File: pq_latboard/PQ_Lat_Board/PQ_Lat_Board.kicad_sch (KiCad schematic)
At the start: 20 parts, among them IC1 TCN75AVOA713, J1 Conn_01x11_MountingPin, J2 connector-coax

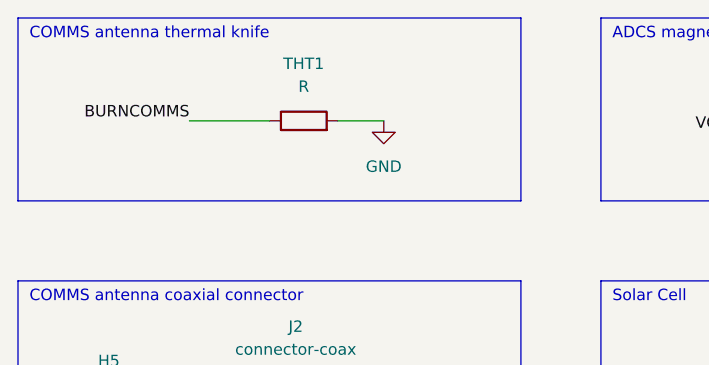
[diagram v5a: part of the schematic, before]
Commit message: BOM creation schematic changes 2.0
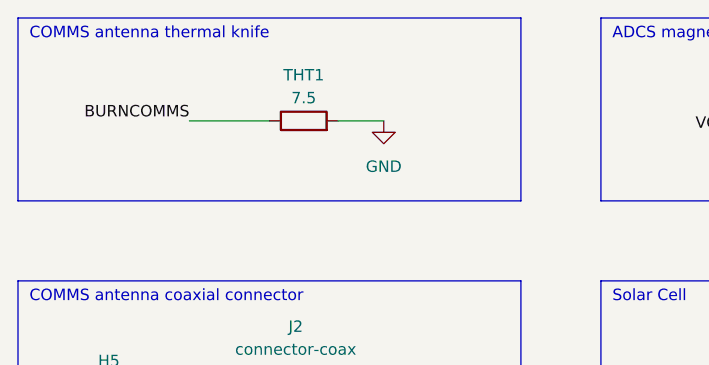
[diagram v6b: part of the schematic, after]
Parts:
- D1: Manufacturer 1 (none) -> Advanced Photonix; Manufacturer Part Number 1 (none) -> SLCD-61N8; Supplier 1 (none) -> Farnell; Supplier Part Number 1 (none) -> 1218991
- H1, H2, H3, H4, H5, NT1: Manufacturer 1 (none) -> N/A; Manufacturer Part Number 1 (none) -> N/A; Supplier 1 (none) -> N/A; Supplier Part Number 1 (none) -> N/A
- IC1: Manufacturer 1 (none) -> Microchip; Manufacturer Part Number 1 (none) -> TCN75AVOA; Supplier 1 (none) -> Mouser; Supplier Part Number 1 (none) -> 579-TCN75AVOA
- J1: Manufacturer 1 (none) -> Molex; Manufacturer Part Number 1 (none) -> PicoBlade_53261; Supplier 1 (none) -> Mouser; Supplier Part Number 1 (none) -> 538-53261-7006
- J2: Manufacturer 1 (none) -> Hirose; Manufacturer Part Number 1 (none) -> C.FL-R-SMT-1; Supplier 1 (none) -> Mouser; Supplier Part Number 1 (none) -> 798-CFL-R-SMT-190
- SC1: Manufacturer 1 (none) -> Azur Space; Manufacturer Part Number 1 (none) -> 3G30A; Supplier 1 (none) -> Lighttricity; Supplier Part Number 1 (none) -> N/A
- THT1: value R -> 7.5; Manufacturer 1 (none) -> Vishay/Dale; Manufacturer Part Number 1 (none) -> MRS25000C7508FCT00; Supplier 1 (none) -> Mouser; Supplier Part Number 1 (none) -> 594-MRS25000C7508FCT
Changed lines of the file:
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@@
   (symbol (lib_id "Device:R") (at 81.28 64.77 90) (unit 1)
     (in_bom yes) (on_board yes) (dnp no) (fields_autoplaced)
-    (property "Reference" "THT1" (at 81.28 58.42 90)
-      (effects (font (size 1.27 1.27)))
-    )
-    (property "Value" "R" (at 81.28 60.96 90)
+    (property "Reference" "THT1" (at 81.28 59.69 90)
+      (effects (font (size 1.27 1.27)))
+    )
+    (property "Value" "7.5" (at 81.28 62.23 90)
       (effects (font (size 1.27 1.27)))
     )
@@
     )
     (property "Datasheet" "~" (at 81.28 64.77 0)
+      (effects (font (size 1.27 1.27)) hide)
+    )
+    (property "Manufacturer 1" "Vishay/Dale" (at 81.28 64.77 0)
+      (effects (font (size 1.27 1.27)) hide)
+    )
+    (property "Manufacturer Part Number 1" "MRS25000C7508FCT00 " (at 81.28 64.77 0)
+      (effects (font (size 1.27 1.27)) hide)
+    )
+    (property "Supplier 1" "Mouser" (at 81.28 64.77 0)
+      (effects (font (size 1.27 1.27)) hide)
+    )
+    (property "Supplier Part Number 1" "594-MRS25000C7508FCT " (at 81.28 64.77 0)
       (effects (font (size 1.27 1.27)) hide)
     )
@@
       (effects (font (size 1.27 1.27)) hide)
     )
+    (property "Manufacturer 1" "N/A" (at 55.88 95.25 0)
+      (effects (font (size 1.27 1.27)) hide)
+    )
+    (property "Manufacturer Part Number 1" "N/A" (at 55.88 95.25 0)
+      (effects (font (size 1.27 1.27)) hide)
+    )
+    (property "Supplier 1" "N/A" (at 55.88 95.25 0)
+      (effects (font (size 1.27 1.27)) hide)
+    )
+    (property "Supplier Part Number 1" "N/A" (at 55.88 95.25 0)
+      (effects (font (size 1.27 1.27)) hide)
+    )
     (pin "1")
     (instances
@@
       (effects (font (size 1.27 1.27)) hide)
     )
+    (property "Manufacturer 1" "N/A" (at 82.55 120.65 0)
+      (effects (font (size 1.27 1.27)) hide)
+    )
+    (property "Manufacturer Part Number 1" "N/A" (at 82.55 120.65 0)
+      (effects (font (size 1.27 1.27)) hide)
+    )
+    (property "Supplier 1" "N/A" (at 82.55 120.65 0)
+      (effects (font (size 1.27 1.27)) hide)
+    )
+    (property "Supplier Part Number 1" "N/A" (at 82.55 120.65 0)
+      (effects (font (size 1.27 1.27)) hide)
+    )
     (pin "1")
     (instances
@@
     )
     (property "Datasheet" "" (at 140.97 103.124 0)
+      (effects (font (size 1.27 1.27)) hide)
+    )
+    (property "Manufacturer 1" "Azur Space" (at 142.494 92.71 0)
+      (effects (font (size 1.27 1.27)) hide)
+    )
+    (property "Manufacturer Part Number 1" "3G30A" (at 142.494 92.71 0)
+      (effects (font (size 1.27 1.27)) hide)
+    )
+    (property "Supplier 1" "Lighttricity" (at 142.494 92.71 0)
+      (effects (font (size 1.27 1.27)) hide)
+    )
+    (property "Supplier Part Number 1" "N/A" (at 142.494 92.71 0)
       (effects (font (size 1.27 1.27)) hide)
     )
@@
       (effects (font (size 1.27 1.27)) hide)
     )
+    (property "Manufacturer 1" "N/A" (at 58.42 134.62 0)
+      (effects (font (size 1.27 1.27)) hide)
+    )
+    (property "Manufacturer Part Number 1" "N/A" (at 58.42 134.62 0)
+      (effects (font (size 1.27 1.27)) hide)
+    )
+    (property "Supplier 1" "N/A" (at 58.42 134.62 0)
+      (effects (font (size 1.27 1.27)) hide)
+    )
+    (property "Supplier Part Number 1" "N/A" (at 58.42 134.62 0)
+      (effects (font (size 1.27 1.27)) hide)
+    )
     (pin "1")
     (instances
@@
     (property "BOM_MANUFACTURER PART" "" (at 190.5 109.22 0)
       (effects (font (size 1.27 1.27)) (justify left bottom) hide)
+    )
+    (property "Manufacturer 1" "Microchip" (at 190.5 109.22 0)
+      (effects (font (size 1.27 1.27)) hide)
+    )
+    (property "Manufacturer Part Number 1" "TCN75AVOA" (at 190.5 109.22 0)
+      (effects (font (size 1.27 1.27)) hide)
+    )
+    (property "Supplier 1" "Mouser" (at 190.5 109.22 0)
+      (effects (font (size 1.27 1.27)) hide)
+    )
+    (property "Supplier Part Number 1" " 579-TCN75AVOA" (at 190.5 109.22 0)
+      (effects (font (size 1.27 1.27)) hide)
     )
     (pin "1")
@@
       (effects (font (size 1.27 1.27)) hide)
     )
+    (property "Manufacturer 1" "N/A" (at 82.55 134.62 0)
+      (effects (font (size 1.27 1.27)) hide)
+    )
+    (property "Manufacturer Part Number 1" "N/A" (at 82.55 134.62 0)
+      (effects (font (size 1.27 1.27)) hide)
+    )
+    (property "Supplier 1" "N/A" (at 82.55 134.62 0)
+      (effects (font (size 1.27 1.27)) hide)
+    )
+    (property "Supplier Part Number 1" "N/A" (at 82.55 134.62 0)
+      (effects (font (size 1.27 1.27)) hide)
+    )
     (pin "1")
     (instances
@@
       (effects (font (size 1.27 1.27)) hide)
     )
+    (property "Manufacturer 1" "N/A" (at 143.51 66.04 0)
+      (effects (font (size 1.27 1.27)) hide)
+    )
+    (property "Manufacturer Part Number 1" "N/A" (at 143.51 66.04 0)
+      (effects (font (size 1.27 1.27)) hide)
+    )
+    (property "Supplier 1" "N/A" (at 143.51 66.04 0)
+      (effects (font (size 1.27 1.27)) hide)
+    )
+    (property "Supplier Part Number 1" "N/A" (at 143.51 66.04 0)
+      (effects (font (size 1.27 1.27)) hide)
+    )
     (pin "1")
     (pin "2")
@@
       (effects (font (size 1.27 1.27)) hide)
     )
+    (property "Manufacturer 1" "N/A" (at 58.42 120.65 0)
+      (effects (font (size 1.27 1.27)) hide)
+    )
+    (property "Manufacturer Part Number 1" "N/A" (at 58.42 120.65 0)
+      (effects (font (size 1.27 1.27)) hide)
+    )
+    (property "Supplier 1" "N/A" (at 58.42 120.65 0)
+      (effects (font (size 1.27 1.27)) hide)
+    )
+    (property "Supplier Part Number 1" "N/A" (at 58.42 120.65 0)
+      (effects (font (size 1.27 1.27)) hide)
+    )
     (pin "1")
     (instances
@@
       (effects (font (size 1.27 1.27)) hide)
     )
+    (property "Manufacturer 1" "Advanced Photonix" (at 214.376 64.77 0)
+      (effects (font (size 1.27 1.27)) hide)
+    )
+    (property "Manufacturer Part Number 1" "SLCD-61N8" (at 214.376 64.77 0)
+      (effects (font (size 1.27 1.27)) hide)
+    )
+    (property "Supplier 1" "Farnell" (at 214.376 64.77 0)
+      (effects (font (size 1.27 1.27)) hide)
+    )
+    (property "Supplier Part Number 1" "1218991" (at 214.376 64.77 0)
+      (effects (font (size 1.27 1.27)) hide)
+    )
     (pin "1")
     (pin "2")
@@
     )
     (property "Datasheet" "~" (at 139.7 129.54 0)
+      (effects (font (size 1.27 1.27)) hide)
+    )
+    (property "Manufacturer 1" "Molex" (at 139.7 129.54 0)
+      (effects (font (size 1.27 1.27)) hide)
+    )
+    (property "Manufacturer Part Number 1" "PicoBlade_53261" (at 139.7 129.54 0)
+      (effects (font (size 1.27 1.27)) hide)
+    )
+    (property "Supplier 1" "Mouser" (at 139.7 129.54 0)
+      (effects (font (size 1.27 1.27)) hide)
+    )
+    (property "Supplier Part Number 1" "538-53261-7006" (at 139.7 129.54 0)
       (effects (font (size 1.27 1.27)) hide)
     )
@@
       (effects (font (size 1.27 1.27)) hide)
     )
+    (property "Manufacturer 1" "Hirose" (at 80.01 93.98 0)
+      (effects (font (size 1.27 1.27)) hide)
+    )
+    (property "Manufacturer Part Number 1" "C.FL-R-SMT-1" (at 80.01 93.98 0)
+      (effects (font (size 1.27 1.27)) hide)
+    )
+    (property "Supplier 1" "Mouser" (at 80.01 93.98 0)
+      (effects (font (size 1.27 1.27)) hide)
+    )
+    (property "Supplier Part Number 1" "798-CFL-R-SMT-190 " (at 80.01 93.98 0)
+      (effects (font (size 1.27 1.27)) hide)
+    )

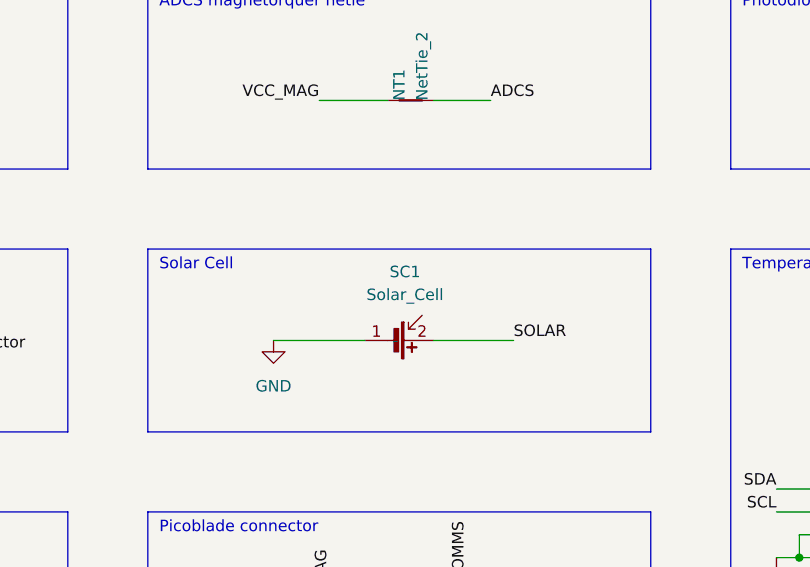
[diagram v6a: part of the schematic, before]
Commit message: Updated outer boards design as required by the change from Azur Space house-cut solar cells to Lighttricity's S3040_CIC model. Preserved the older design in lat_board_old
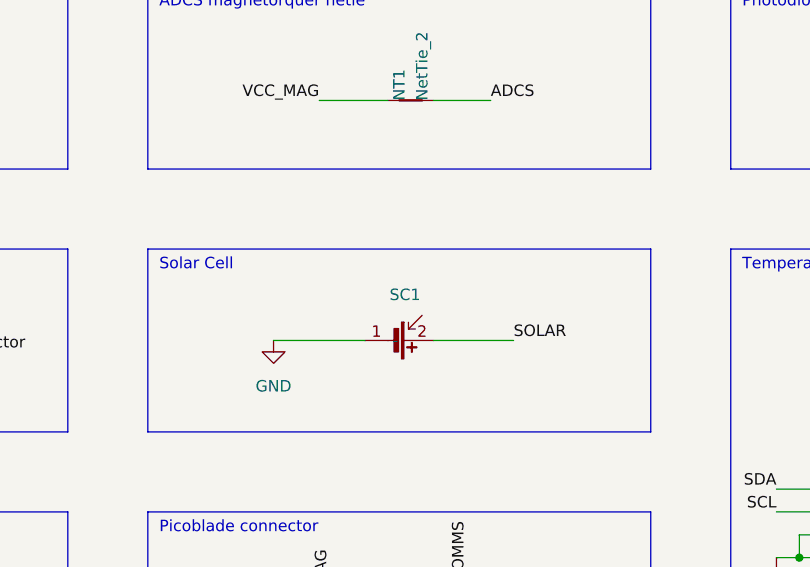
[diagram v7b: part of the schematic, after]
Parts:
- removed SC1: Solar_Cell, -nsl_power:Azur-Space-PQ-cut-SC, symbol power-nsl:Solar_Cell
- added SC1: ~, power-nsl:Lighttricity_S3040_CIC, symbol power-nsl:S3040_CIC
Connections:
- net GND: now also SC1.1 (-)
- net SOLAR: now also SC1.2
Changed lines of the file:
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@@
-    )
-  )
-  (symbol (lib_id "power-nsl:Solar_Cell") (at 142.494 92.71 270) (unit 1)
-    (in_bom yes) (on_board yes) (dnp no) (fields_autoplaced)
-    (property "Reference" "SC1" (at 142.875 85.09 90)
-      (effects (font (size 1.27 1.27)))
-    )
-    (property "Value" "Solar_Cell" (at 142.875 87.63 90)
-      (effects (font (size 1.27 1.27)))
-    )
-    (property "Footprint" "-nsl_power:Azur-Space-PQ-cut-SC" (at 140.97 103.124 0)
-      (effects (font (size 1.27 1.27)) hide)
-    )
-    (property "Datasheet" "" (at 140.97 103.124 0)
-      (effects (font (size 1.27 1.27)) hide)
-    )
-    (property "Manufacturer 1" "Azur Space" (at 142.494 92.71 0)
-      (effects (font (size 1.27 1.27)) hide)
-    )
-    (property "Manufacturer Part Number 1" "3G30A" (at 142.494 92.71 0)
-      (effects (font (size 1.27 1.27)) hide)
-    )
-    (property "Supplier 1" "Lighttricity" (at 142.494 92.71 0)
-      (effects (font (size 1.27 1.27)) hide)
-    )
-    (property "Supplier Part Number 1" "N/A" (at 142.494 92.71 0)
-      (effects (font (size 1.27 1.27)) hide)
-    )
-    (pin "1")
-    (pin "2")
-    (instances
-      (project "PQ_Lat_Board"
-        (path "/4da848d5-e65a-4ace-88f8-d9d6d6b9afa2"
-          (reference "SC1") (unit 1)
-        )
-      )
     )
   )
@@
         )
       )
+    )
+  )
+  (symbol (lib_id "power-nsl:S3040_CIC") (at 142.24 92.71 270) (unit 1)
+    (in_bom yes) (on_board yes) (dnp no) (fields_autoplaced)
+    (property "Reference" "SC1" (at 142.875 87.63 90)
+      (effects (font (size 1.27 1.27)))
+    )
+    (property "Value" "~" (at 142.24 92.71 0)
+      (effects (font (size 1.27 1.27)))
+    )
+    (property "Footprint" "power-nsl:Lighttricity_S3040_CIC" (at 142.24 92.71 0)
+      (effects (font (size 1.27 1.27)) hide)
+    )
+    (property "Datasheet" "" (at 142.24 92.71 0)
+      (effects (font (size 1.27 1.27)) hide)
+    )
+    (pin "1")
+    (pin "2")
+    (instances
+      (project "PQ_Lat_Board"
+        (path "/4da848d5-e65a-4ace-88f8-d9d6d6b9afa2"
+          (reference "SC1") (unit 1)
+        )
+      )

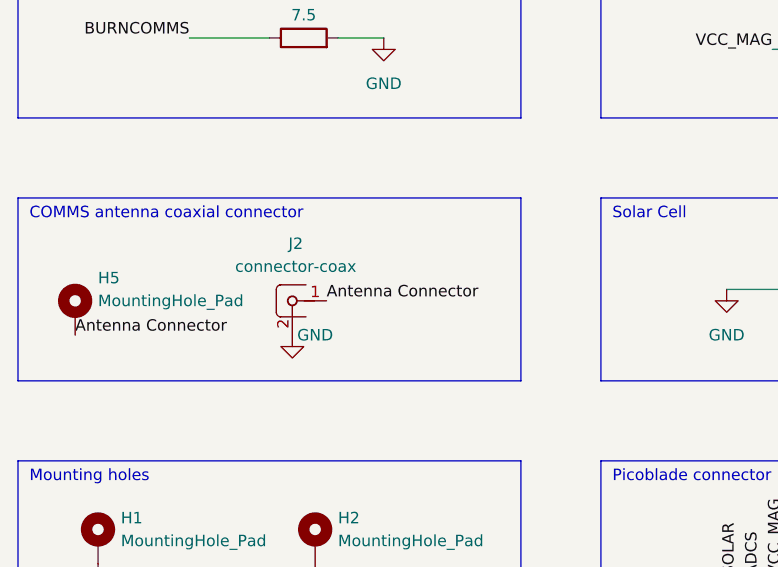
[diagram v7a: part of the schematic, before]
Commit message: solved wrong connector in lateral board
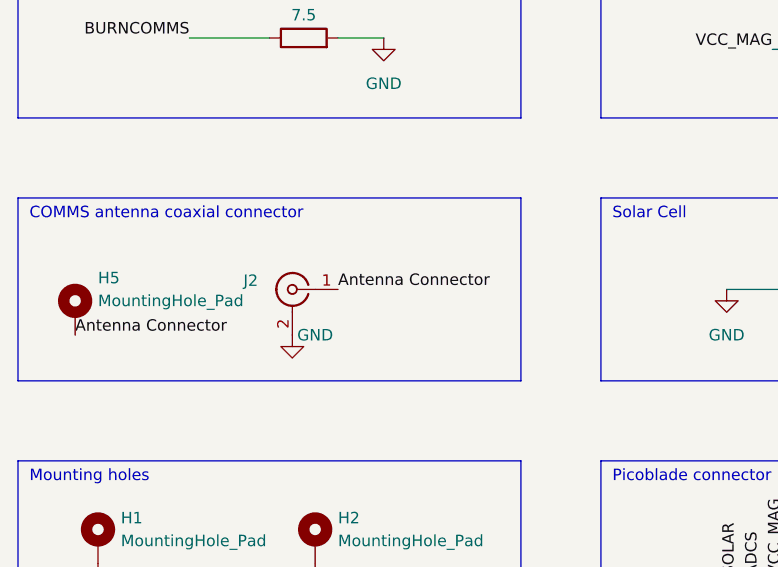
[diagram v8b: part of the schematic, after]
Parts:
- removed J2: connector-coax, -nsl_connector:C.FL-R-SMT-1(90), symbol connector-nsl:connector-coax
- added J2: Conn_Coaxial, Connector_Coaxial:U.FL_Hirose_U.FL-R-SMT-1_Vertical, symbol Connector:Conn_Coaxial
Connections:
- net Antenna Connector: now also J2.1 (In)
- net GND: now also J2.2 (Ext)
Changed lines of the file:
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@@
     (effects (font (size 1.27 1.27)) (justify right bottom))
   )
-  (label "Antenna Connector" (at 83.82 93.98 0) (fields_autoplaced)
+  (label "Antenna Connector" (at 85.09 92.71 0) (fields_autoplaced)
     (effects (font (size 1.27 1.27)) (justify left bottom))
   )
@@
         (path "/4da848d5-e65a-4ace-88f8-d9d6d6b9afa2"
           (reference "#PWR0107") (unit 1)
+        )
+      )
+    )
+  )
+  (symbol (lib_id "Connector:Conn_Coaxial") (at 80.01 92.71 0) (mirror y) (unit 1)
+    (in_bom yes) (on_board yes) (dnp no)
+    (property "Reference" "J2" (at 76.2 91.7332 0)
+      (effects (font (size 1.27 1.27)) (justify left))
+    )
+    (property "Value" "Conn_Coaxial" (at 76.2 94.2732 0)
+      (effects (font (size 1.27 1.27)) (justify left) hide)
+    )
+    (property "Footprint" "Connector_Coaxial:U.FL_Hirose_U.FL-R-SMT-1_Vertical" (at 80.01 92.71 0)
+      (effects (font (size 1.27 1.27)) hide)
+    )
+    (property "Datasheet" " ~" (at 80.01 92.71 0)
+      (effects (font (size 1.27 1.27)) hide)
+    )
+    (pin "2")
+    (pin "1")
+    (instances
+      (project "PQ_Lat_Board"
+        (path "/4da848d5-e65a-4ace-88f8-d9d6d6b9afa2"
+          (reference "J2") (unit 1)
         )
       )
@@
         )
       )
-    )
-  )
-  (symbol (lib_id "connector-nsl:connector-coax") (at 80.01 93.98 0) (unit 1)
-    (in_bom yes) (on_board yes) (dnp no) (fields_autoplaced)
-    (property "Reference" "J2" (at 80.391 87.63 0)
-      (effects (font (size 1.27 1.27)))
-    )
-    (property "Value" "connector-coax" (at 80.391 90.17 0)
-      (effects (font (size 1.27 1.27)))
-    )
-    (property "Footprint" "-nsl_connector:C.FL-R-SMT-1(90)" (at 80.391 90.17 0)
-      (effects (font (size 1.27 1.27)) hide)
-    )
-    (property "Datasheet" "" (at 81.28 92.71 0)
-      (effects (font (size 1.27 1.27)) hide)
-    )
-    (property "Manufacturer 1" "Hirose" (at 80.01 93.98 0)
-      (effects (font (size 1.27 1.27)) hide)
-    )
-    (property "Manufacturer Part Number 1" "C.FL-R-SMT-1" (at 80.01 93.98 0)
-      (effects (font (size 1.27 1.27)) hide)
-    )
-    (property "Supplier 1" "Mouser" (at 80.01 93.98 0)
-      (effects (font (size 1.27 1.27)) hide)
-    )
-    (property "Supplier Part Number 1" "798-CFL-R-SMT-190 " (at 80.01 93.98 0)
-      (effects (font (size 1.27 1.27)) hide)
-    )
-    (pin "1")
-    (pin "2")
-    (instances
-      (project "PQ_Lat_Board"
-        (path "/4da848d5-e65a-4ace-88f8-d9d6d6b9afa2"
-          (reference "J2") (unit 1)
-        )
-      )
